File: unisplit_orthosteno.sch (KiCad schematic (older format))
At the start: 52 parts

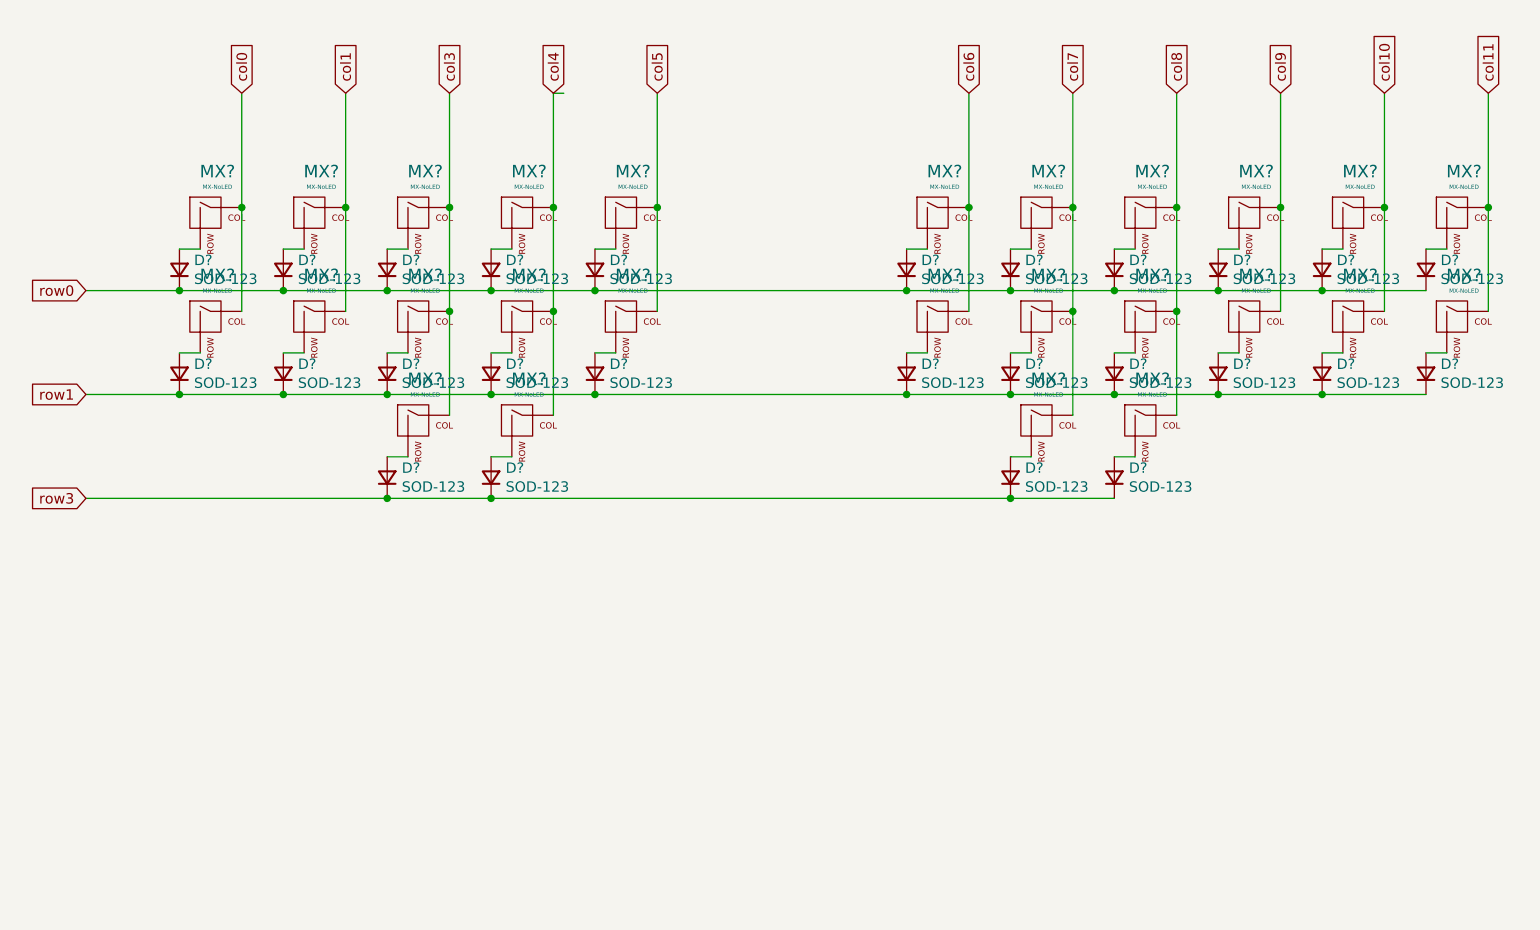
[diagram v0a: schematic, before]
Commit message: finally found pro micro symbol from keebio
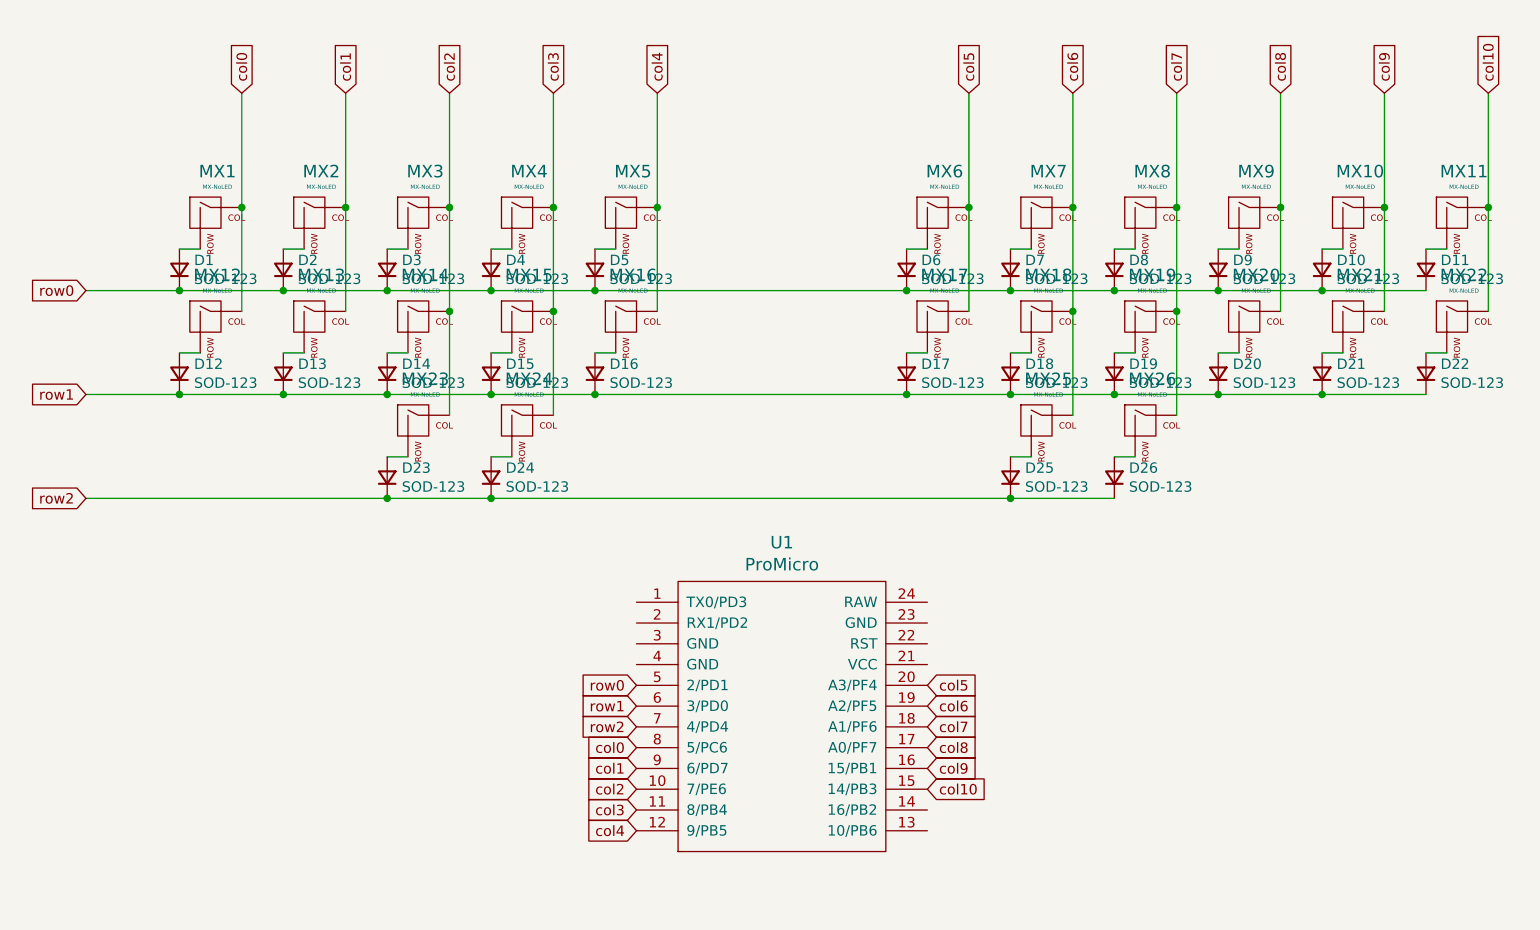
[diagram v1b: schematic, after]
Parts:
- added U1: ProMicro, symbol keebio:ProMicro
- gave numbers to parts that had none: 52
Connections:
- net col11 is gone; now on net col10: MX11.1 (COL), MX22.1 (COL)
- net col0: now also U1.8 (5/PC6)
- net col1: now also U1.9 (6/PD7)
- net col10: now also U1.15 (14/PB3); no longer MX10.1 (COL), MX21.1 (COL)
- net col3: now also MX15.1 (COL), MX24.1 (COL), MX4.1 (COL), U1.11 (8/PB4); no longer MX14.1 (COL), MX23.1 (COL), MX3.1 (COL)
- net col4: now also MX16.1 (COL), MX5.1 (COL), U1.12 (9/PB5); no longer MX15.1 (COL), MX24.1 (COL), MX4.1 (COL)
- net col5: now also MX17.1 (COL), MX6.1 (COL), U1.20 (A3/PF4); no longer MX16.1 (COL), MX5.1 (COL)
- net col6: now also MX18.1 (COL), MX25.1 (COL), MX7.1 (COL), U1.19 (A2/PF5); no longer MX17.1 (COL), MX6.1 (COL)
- net col7: now also MX19.1 (COL), MX26.1 (COL), MX8.1 (COL), U1.18 (A1/PF6); no longer MX18.1 (COL), MX25.1 (COL), MX7.1 (COL)
- net col8: now also MX20.1 (COL), MX9.1 (COL), U1.17 (A0/PF7); no longer MX19.1 (COL), MX26.1 (COL), MX8.1 (COL)
- net col9: now also MX10.1 (COL), MX21.1 (COL), U1.16 (15/PB1); no longer MX20.1 (COL), MX9.1 (COL)
- net row0: now also U1.5 (2/PD1)
- net row1: now also U1.6 (3/PD0)
- net row3 renamed row2
- net row2: now also U1.7 (4/PD4)
- new net col2: MX14.1 (COL), MX23.1 (COL), MX3.1 (COL), U1.10 (7/PE6)

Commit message: assign footprints and do some organizing
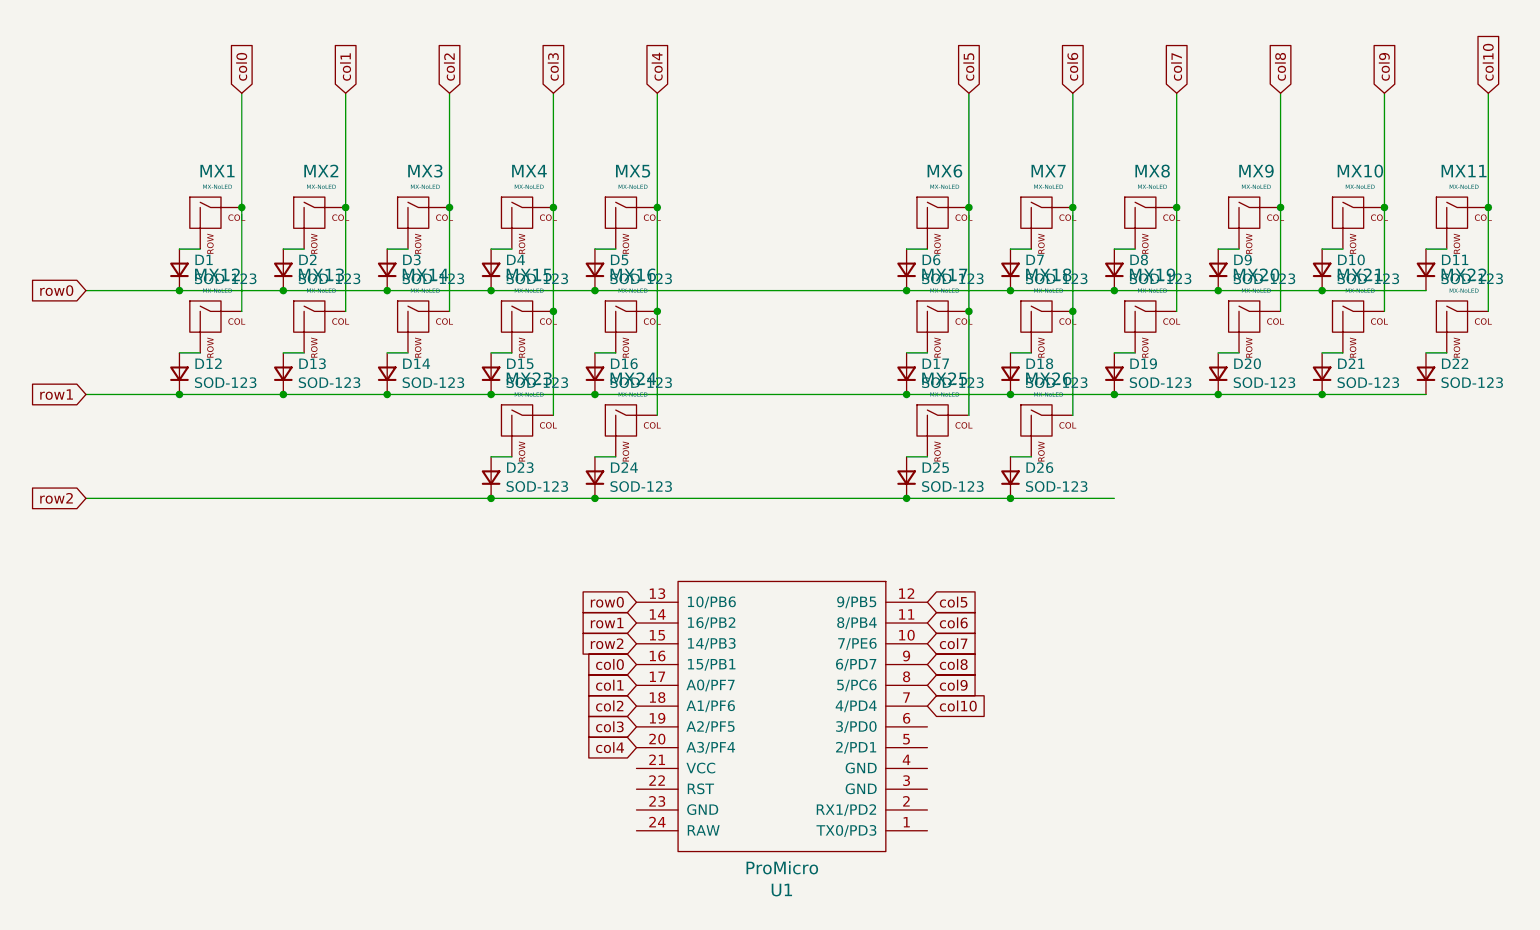
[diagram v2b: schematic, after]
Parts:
- D1, D10, D11, D12, D13, D14, D15, D16, D17, D18, D19, D2, D20, D21, D22, D23, D24, D25, D26, D3, D4, D5, D6, D7, D8, D9: footprint (none) -> Keebio-Parts:D_SOD123
- MX1, MX10, MX11, MX12, MX13, MX14, MX15, MX16, MX17, MX18, MX19, MX2, MX20, MX21, MX22, MX23, MX24, MX25, MX26, MX3, MX4, MX5, MX6, MX7, MX8, MX9: footprint (none) -> Keebio-Parts:MX-Alps-Choc-1U-NoLED
- U1: footprint (none) -> Keebio-Parts:ArduinoProMicro
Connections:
- net col0: now also U1.16 (15/PB1); no longer U1.8 (5/PC6)
- net col1: now also U1.17 (A0/PF7); no longer U1.9 (6/PD7)
- net col10: now also U1.7 (4/PD4); no longer U1.15 (14/PB3)
- net col2: now also U1.18 (A1/PF6); no longer MX23.1 (COL), U1.10 (7/PE6)
- net col3: now also MX23.1 (COL), U1.19 (A2/PF5); no longer MX24.1 (COL), U1.11 (8/PB4)
- net col4: now also MX24.1 (COL), U1.20 (A3/PF4); no longer U1.12 (9/PB5)
- net col5: now also MX25.1 (COL), U1.12 (9/PB5); no longer U1.20 (A3/PF4)
- net col6: now also MX26.1 (COL), U1.11 (8/PB4); no longer MX25.1 (COL), U1.19 (A2/PF5)
- net col7: now also U1.10 (7/PE6); no longer MX26.1 (COL), U1.18 (A1/PF6)
- net col8: now also U1.9 (6/PD7); no longer U1.17 (A0/PF7)
- net col9: now also U1.8 (5/PC6); no longer U1.16 (15/PB1)
- net row0: now also U1.13 (10/PB6); no longer U1.5 (2/PD1)
- net row1: now also U1.14 (16/PB2); no longer U1.6 (3/PD0)
- net row2: now also U1.15 (14/PB3); no longer U1.7 (4/PD4)
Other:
- moved on the sheet: D23, D24, D25, D26, MX23, MX24, MX25, MX26
